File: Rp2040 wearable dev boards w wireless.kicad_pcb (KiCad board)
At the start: 4 copper layers, 40 x 65.7 mm, 79 parts, among them IC1 NRF24L01P-R7, J1 battery plug, J3 Conn_01x20, J4 Conn_01x20, J5 Conn_01x04, J6 EMPCB.SMAFSTJ.B.HT, Q1 Si2301, SW1 B3U-1100P, SW2 power Switch, U1 MCP73831T-4ADI/OT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

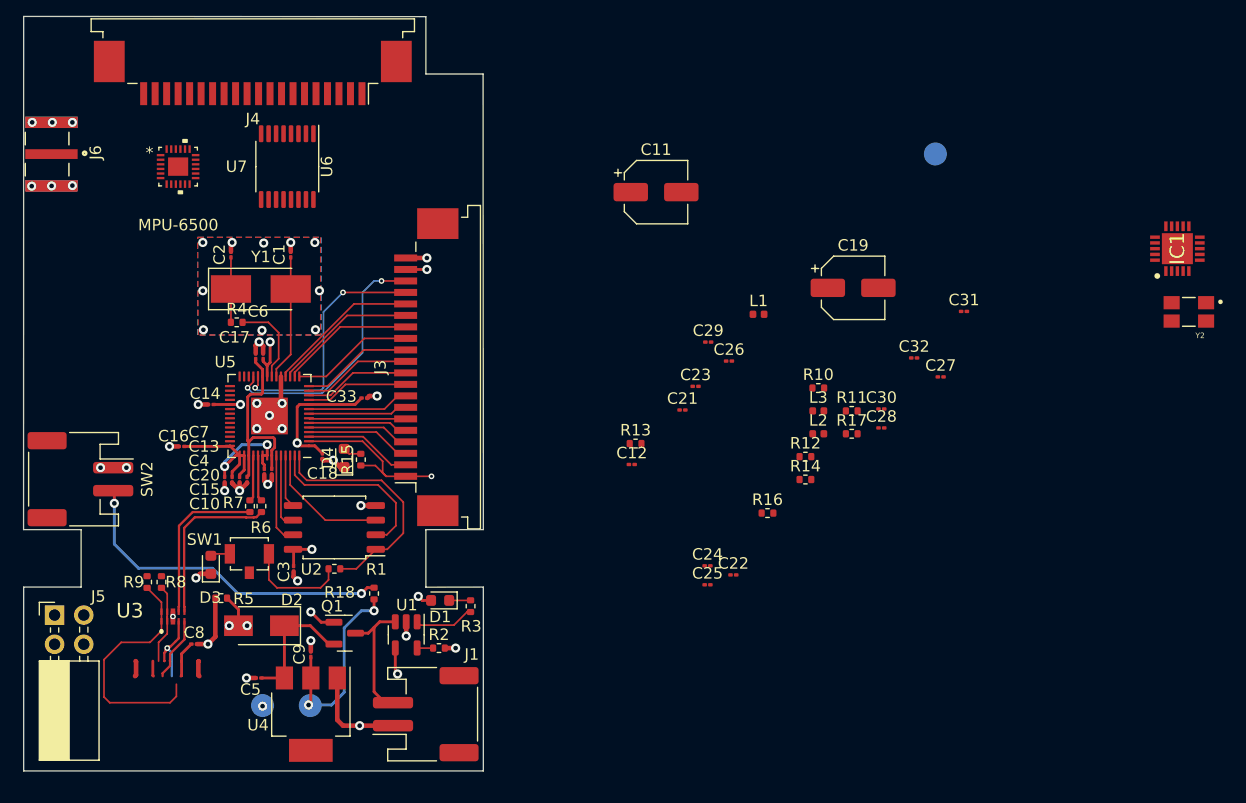
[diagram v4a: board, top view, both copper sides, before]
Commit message: finished pcb route v1, asked the electronics discord if they could verify it.
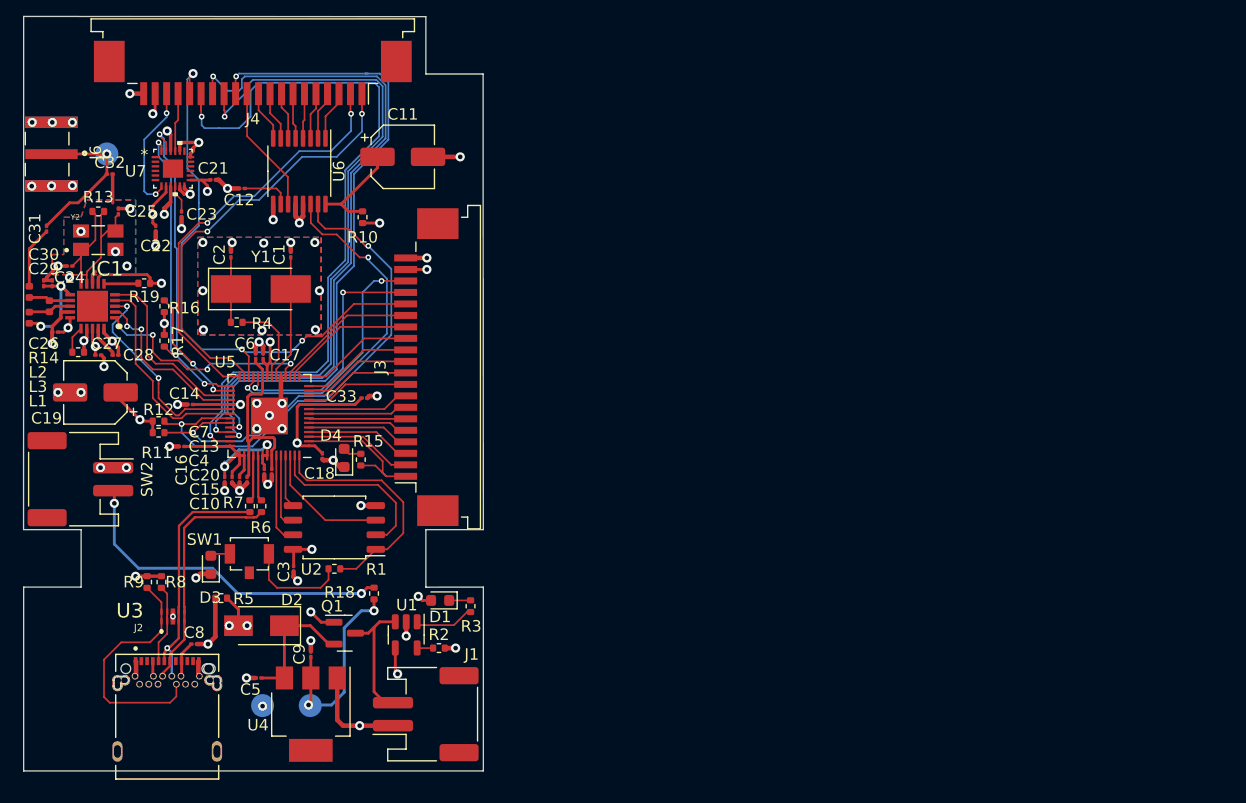
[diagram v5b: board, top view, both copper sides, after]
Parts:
- removed J5: Conn_01x04, Connector_PinSocket_2.54mm:PinSocket_2x02_P2.54mm_Horizontal
- added J2: UJ31-CH-31-SMT-TR, usb-c footprint:CUI_UJ31-CH-31-SMT-TR, F.Cu at (48.5, 90.4)
- added R19: 2K, Resistor_SMD:R_0402_1005Metric, F.Cu at (46.5, 57.5)
- R4: value 1k -> 10k
- moved Y2 95.1 mm to (42.5, 53.8), turned to 0 degrees
- moved IC1 94.5 mm to (42.0, 59.5), turned to 180 degrees
- moved C31 80.2 mm to (38.0, 52.8), turned to 90 degrees
- moved C27 73.3 mm to (42.5, 63.8)
- moved C30 73.0 mm to (38.5, 57.5), turned to 90 degrees
- moved TP3 72.1 mm to (43.2, 46.2)
- moved C32 71.8 mm to (43.5, 48.0)
- moved L2 69.8 mm to (36.5, 58.2), turned to 90 degrees
- moved L3 69.1 mm to (36.5, 60.5), turned to -90 degrees
- moved C28 67.0 mm to (44.0, 63.8)
- moved C19 66.6 mm to (42.2, 67.0), turned to 180 degrees
- moved R14 64.3 mm to (40.8, 63.5), turned to 180 degrees
- moved L1 61.7 mm to (38.2, 59.5), turned to -90 degrees
- moved C24 61.3 mm to (40.0, 56.0), turned to 180 degrees
- moved C25 60.7 mm to (44.2, 51.2), turned to 90 degrees
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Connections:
- IC1 pad 6: /IRQ -> Net-(IC1-Pad6)
- J3 pad 16: /GPIO 15 -> /RUN
- J4 pad 1: /GPIO 0 -> /GPIO 16
- J4 pad 2: /GPIO 16 -> /GPIO 17
- J4 pad 3: /GPIO 17 -> /ACH0
- J4 pad 4: /ACH0 -> /ACH1
- J4 pad 5: /ACH1 -> /ACH2
- J4 pad 6: /ACH2 -> /ACH3
- J4 pad 7: /ACH3 -> /ACH4
- U5 pad 18: /GPIO 15 -> /CE
- U6 pad 15: /External ADC SCL / GPIO 21 -> /External ADC SDA / GPIO 20
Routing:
- net /ADC 4: track 0.00 -> 65.4 mm, vias 0 -> 2
- net /ADC 3: track 0.00 -> 60.1 mm, vias 0 -> 2
- net /ADC 2: track 0.00 -> 59.2 mm, vias 0 -> 2
- net /ADC 1: track 0.00 -> 56.5 mm, vias 0 -> 2
- net /RUN: track 0.00 -> 50.0 mm, vias 0 -> 3
- net GND: track 43.3 -> 89.2 mm, vias 41 -> 65
- net /External ADC SDA / GPIO 20: track 0.00 -> 44.9 mm, vias 0 -> 2
- net /External ADC SCL / GPIO 21: track 0.00 -> 42.3 mm, vias 0 -> 2
- net /Vmain: track 44.7 -> 86.8 mm, vias 9 -> 18
- net /GPIO 16: track 0.00 -> 37.7 mm, vias 0 -> 2
- net /GPIO 17: track 0.00 -> 37.0 mm, vias 0 -> 2
- net /IMU SCL / GPIO 19: track 0.00 -> 33.9 mm, vias 0 -> 3
- net /IMU SDA / GPIO 18: track 0.00 -> 27.1 mm, vias 0 -> 3
- net /CE: track 0.00 -> 20.3 mm, vias 0 -> 4
- net /SCK: track 0.00 -> 18.3 mm, vias 0 -> 2
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- added copper zone on B.Cu, net GND

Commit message: e
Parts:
- TP3: moved to F.Cu
- turned TP3 to 0 degrees
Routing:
- net /Antenna: vias 1 -> 0
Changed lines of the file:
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@@
     )
   )
+  (footprint "TestPoint:TestPoint_Pad_D2.0mm" (layer "F.Cu")
+    (at 43.25 46.25)
+    (descr "SMD pad as test Point, diameter 2.0mm")
+    (tags "test point SMD pad")
+    (property "Sheetfile" "Rp2040 wearable dev boards w wireless.kicad_sch")
+    (property "Sheetname" "")
+    (attr exclude_from_pos_files)
+    (fp_text reference "TP3" (at 0 -1.998) (layer "F.SilkS")
+      (effects (font (size 1 1) (thickness 0.15)))
+    )
+    (fp_text value "rf test point" (at 0 2.05) (layer "F.Fab")
+      (effects (font (size 1 1) (thickness 0.15)))
+    )
+    (fp_text user "${REFERENCE}" (at 0 -2) (layer "F.Fab")
+      (effects (font (size 1 1) (thickness 0.15)))
+    )
+    (fp_circle (center 0 0) (end 0 1.2) (layer "F.SilkS") (width 0.12) (fill none))
+    (fp_circle (center 0 0) (end 1.5 0) (layer "F.CrtYd") (width 0.05) (fill none))
+    (pad "1" smd circle (at 0 0) (size 2 2) (layers "F.Cu" "F.Mask")
+      (net 1 "/Antenna") (pinfunction "1") (pintype "passive"))
+  )
   (footprint "Capacitor_SMD:C_01005_0402Metric" (layer "F.Cu")
     (at 38 52.75 90)
@@
   )
   (footprint "TestPoint:TestPoint_Pad_D2.0mm" (layer "B.Cu")
-    (at 43.25 46.25 180)
-    (descr "SMD pad as test Point, diameter 2.0mm")
-    (tags "test point SMD pad")
-    (property "Sheetfile" "Rp2040 wearable dev boards w wireless.kicad_sch")
-    (property "Sheetname" "")
-    (attr exclude_from_pos_files)
-    (fp_text reference "TP3" (at 0 1.998) (layer "B.SilkS")
-      (effects (font (size 1 1) (thickness 0.15)) (justify mirror))
-    )
-    (fp_text value "rf test point" (at 0 -2.05) (layer "B.Fab")
-      (effects (font (size 1 1) (thickness 0.15)) (justify mirror))
-    )
-    (fp_text user "${REFERENCE}" (at 0 2) (layer "B.Fab")
-      (effects (font (size 1 1) (thickness 0.15)) (justify mirror))
-    )
-    (fp_circle (center 0 0) (end 0 -1.2) (layer "B.SilkS") (width 0.12) (fill none))
-    (fp_circle (center 0 0) (end 1.5 0) (layer "B.CrtYd") (width 0.05) (fill none))
-    (pad "1" smd circle (at 0 0 180) (size 2 2) (layers "B.Cu" "B.Mask")
-      (net 1 "/Antenna") (pinfunction "1") (pintype "passive"))
-  )
-  (footprint "TestPoint:TestPoint_Pad_D2.0mm" (layer "B.Cu")
     (at 60.95 94.25 180)
     (descr "SMD pad as test Point, diameter 2.0mm")
@@
   (segment (start 40.75 50.5) (end 43.25 48) (width 0.25) (layer "F.Cu") (net 1))
   (segment (start 38 52.5) (end 40 50.5) (width 0.25) (layer "F.Cu") (net 1))
-  (via (at 43.25 46.25) (size 0.8) (drill 0.4) (layers "F.Cu" "B.Cu") (net 1))
   (segment (start 59.25 58) (end 59.25 55.25) (width 0.15) (layer "F.Cu") (net 2))
   (segment (start 58 65.6125) (end 58 64.95) (width 0.15) (layer "F.Cu") (net 2))
